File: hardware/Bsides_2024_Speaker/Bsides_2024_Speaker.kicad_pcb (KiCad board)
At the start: 2 copper layers, 144.4 x 144.3 mm, 45 parts, among them J1 Add_On, J2 Battery, J3 Battery, J4 OLED, J5 Serial_IN, J6 Serial_OUT, P1 USB_C_Plug_USB2.0, Q1 DMG3415U-7, SW1 ON, SW2 RESET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

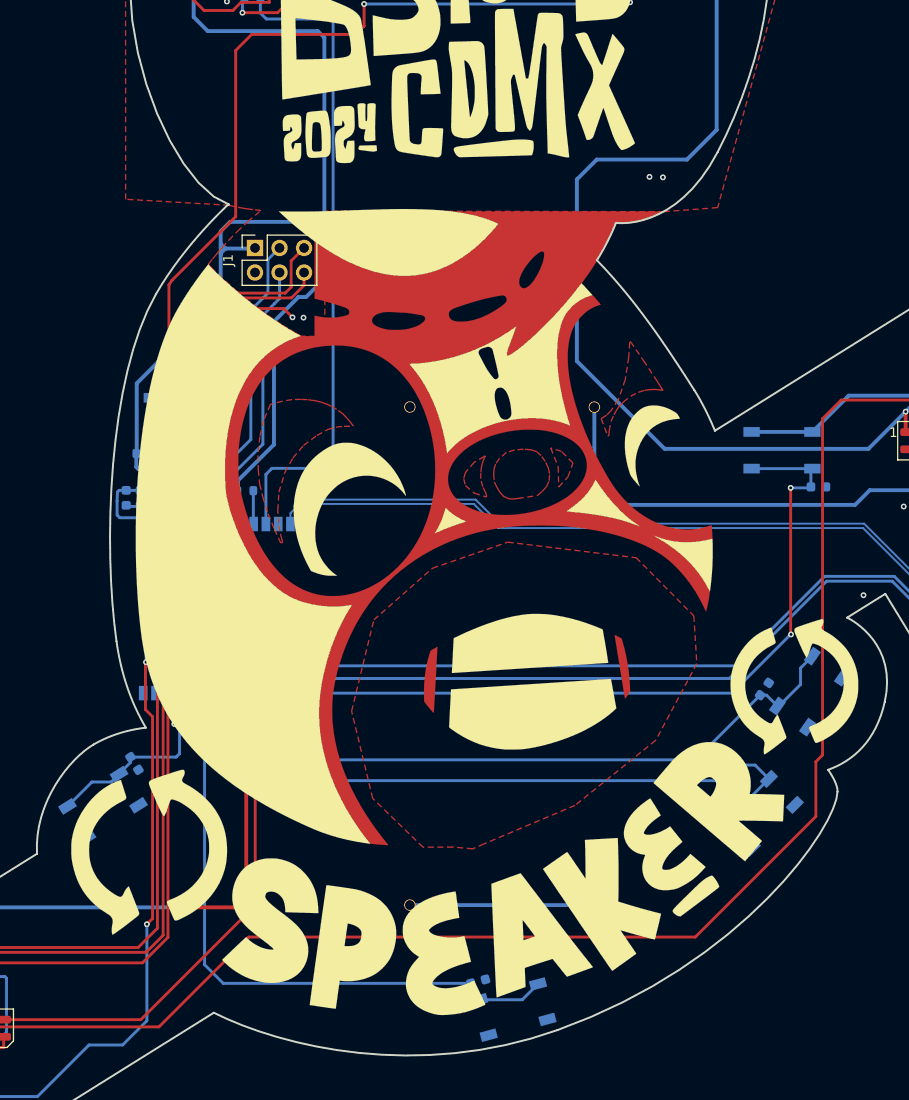
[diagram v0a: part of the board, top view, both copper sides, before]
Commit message: feat(Hw):Moved_Buttons_Speaker
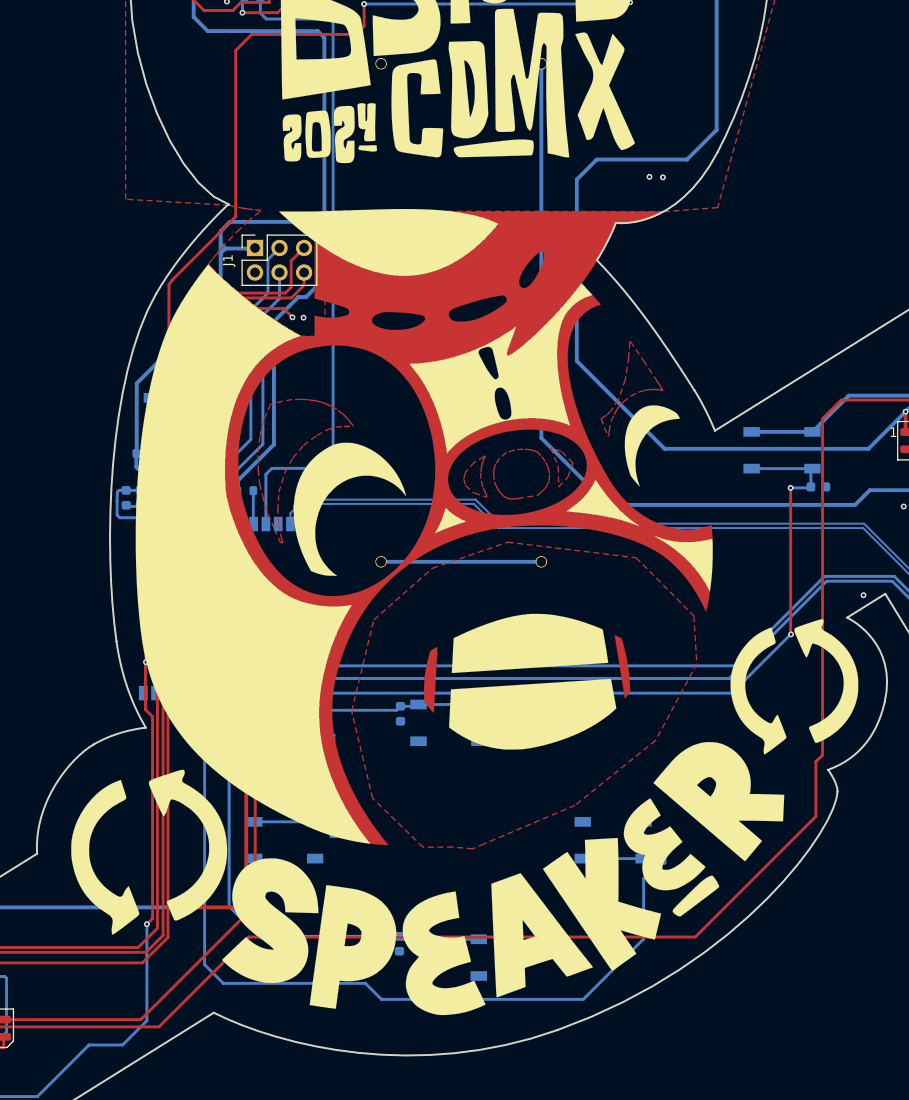
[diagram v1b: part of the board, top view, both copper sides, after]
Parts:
- moved C10 37.8 mm to (137.0, 120.1), turned to 90 degrees
- moved SW6 37.5 mm to (142.0, 121.0), turned to 0 degrees
- moved C11 37.5 mm to (136.9, 143.9), turned to 90 degrees
- moved J2 36.0 mm to (151.6, 78.6)
- moved J3 35.7 mm to (135.0, 78.6)
- moved SW7 35.6 mm to (141.9, 145.3), turned to 0 degrees
- moved C9 23.2 mm to (164.1, 134.5), turned to -90 degrees
- moved C8 21.7 mm to (130.1, 131.7), turned to 90 degrees
- moved SW5 20.3 mm to (159.0, 133.2), turned to 180 degrees
- moved SW4 19.1 mm to (125.0, 133.2), turned to 0 degrees
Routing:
- net /GPIO22: track 71.8 -> 26.5 mm
- net +BATT: track 51.1 -> 88.9 mm
- net /GPIO15: track 65.3 -> 94.8 mm
- net /GPIO23: track 71.1 -> 49.4 mm
- net /GPIO1: track 42.9 -> 59.3 mm
- net Net-(J2-Pin_1): track 19.1 -> 16.6 mm

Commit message: feat(Hw):Update_Csv_Speaker
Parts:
- added kibuzzard-666B311C: G***, kibuzzard-666B311C, B.Cu at (201.1, 97.0)
- added kibuzzard-666B3128: G***, kibuzzard-666B3128, F.Cu at (201.1, 97.0)
- added kibuzzard-666B314A: G***, kibuzzard-666B314A, F.Cu at (196.7, 89.8)
- added kibuzzard-666B316E: G***, kibuzzard-666B316E, B.Cu at (196.7, 89.7)
- added kibuzzard-666B3243: G***, kibuzzard-666B3243, B.Cu at (142.0, 124.8)
- added kibuzzard-666B3258: G***, kibuzzard-666B3258, B.Cu at (141.8, 141.4)
- added kibuzzard-666B327A: G***, kibuzzard-666B327A, B.Cu at (131.2, 134.0)
- added kibuzzard-666B328D: G***, kibuzzard-666B328D, B.Cu at (152.3, 133.0)
- F1: value 0.5A -> 0.75A
- SW2, SW4, SW6: value RESET -> SW
- SW5, SW7: value ~ -> SW
- moved J1 0.14 mm to (121.8, 71.8)
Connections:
- net /GPIO1 renamed /LEFT
- net /GPIO15 renamed /RIGHT
- net /GPIO16 renamed /TX
- net /GPIO17 renamed /RX
- net /GPIO22 renamed /UP
- net /GPIO23 renamed /DOWN
- net /GPIO4 renamed /RX1
- net /GPIO5 renamed /TX1
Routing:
- net GND: track 132.7 -> 122.7 mm

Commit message: feat(Hw): Update BOM
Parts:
- removed kibuzzard-666B3128: G***, kibuzzard-666B3128
- removed kibuzzard-666B314A: G***, kibuzzard-666B314A
- added kibuzzard-666B558C: G***, kibuzzard-666B558C, B.Cu at (176.4, 88.8)
- added kibuzzard-666B55CA: G***, kibuzzard-666B55CA, B.Cu at (152.3, 133.0)
- added kibuzzard-666B5A62: G***, kibuzzard-666B5A62, F.Cu at (203.7, 117.5)
- added kibuzzard-666B5A62: G***, kibuzzard-666B5A62, B.Cu at (84.4, 157.9)
- added kibuzzard-666B5A91: G***, kibuzzard-666B5A91, F.Cu at (206.2, 116.1)
- added kibuzzard-666B5A91: G***, kibuzzard-666B5A91, B.Cu at (85.7, 160.0)
- added kibuzzard-666B5AA1: G***, kibuzzard-666B5AA1, F.Cu at (208.1, 114.5)
- added kibuzzard-666B5AA1: G***, kibuzzard-666B5AA1, B.Cu at (83.3, 155.4)
- added kibuzzard-666B5BCA: G***, kibuzzard-666B5BCA, F.Cu at (121.7, 68.8)
- added kibuzzard-666B5C0A: G***, kibuzzard-666B5C0A, F.Cu at (121.7, 76.5)
- added kibuzzard-666B5C24: G***, kibuzzard-666B5C24, F.Cu at (124.3, 68.7)
- added kibuzzard-666B5C33: G***, kibuzzard-666B5C33, F.Cu at (124.3, 77.3)
- moved kibuzzard-666B328D 61.0 mm to (114.3, 85.4)
- moved J2 2.86 mm to (153.9, 76.9)
- moved J3 2.86 mm to (137.3, 76.9)
- moved D3 0.49 mm to (164.4, 41.4)
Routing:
- net GND: track 122.7 -> 116.1 mm, vias 11 -> 9
- net /VOUT: track 421.3 -> 424.4 mm
- net /RIGHT: track 94.8 -> 96.0 mm
- net +BATT: track 88.9 -> 89.6 mm
- net Net-(D4-DOUT): track 158.0 -> 158.6 mm
- net Net-(D3-DOUT): track 180.7 -> 180.2 mm

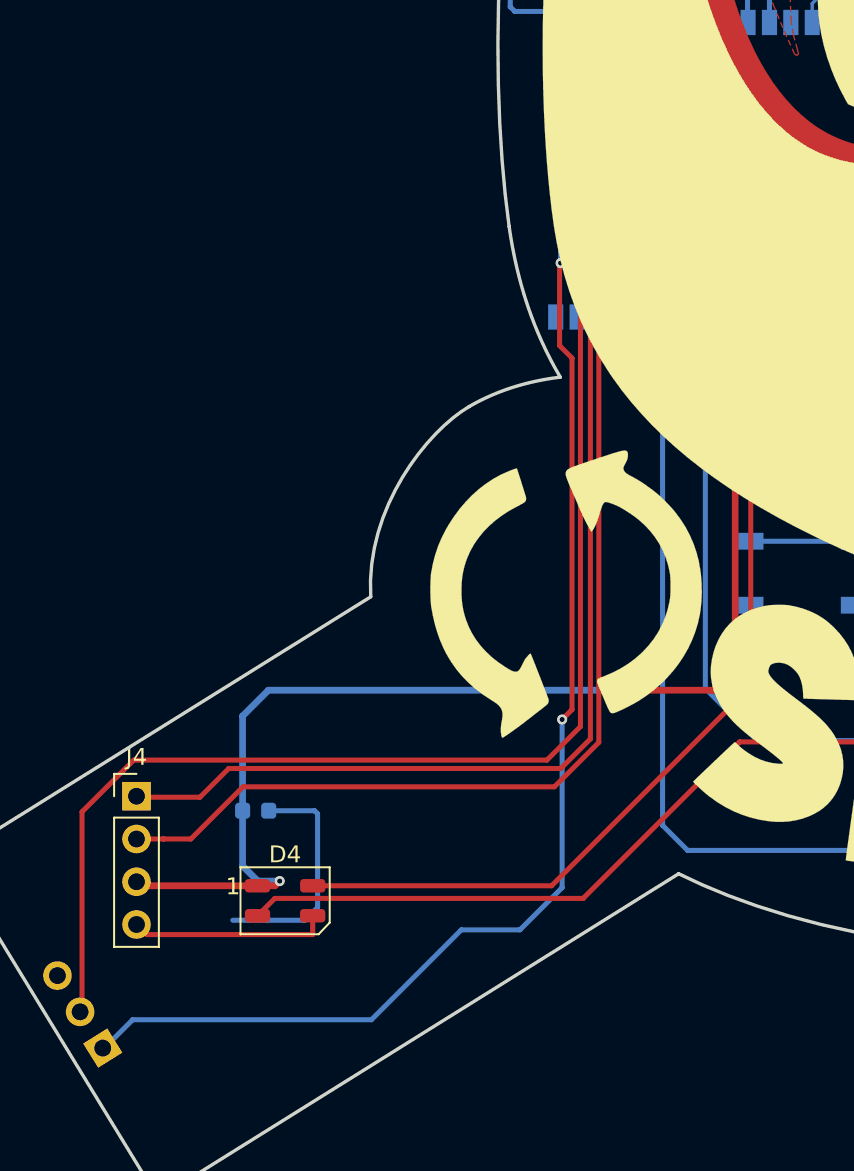
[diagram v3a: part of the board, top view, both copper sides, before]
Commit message: feat(Hw): Update route Speaker and Sponsor
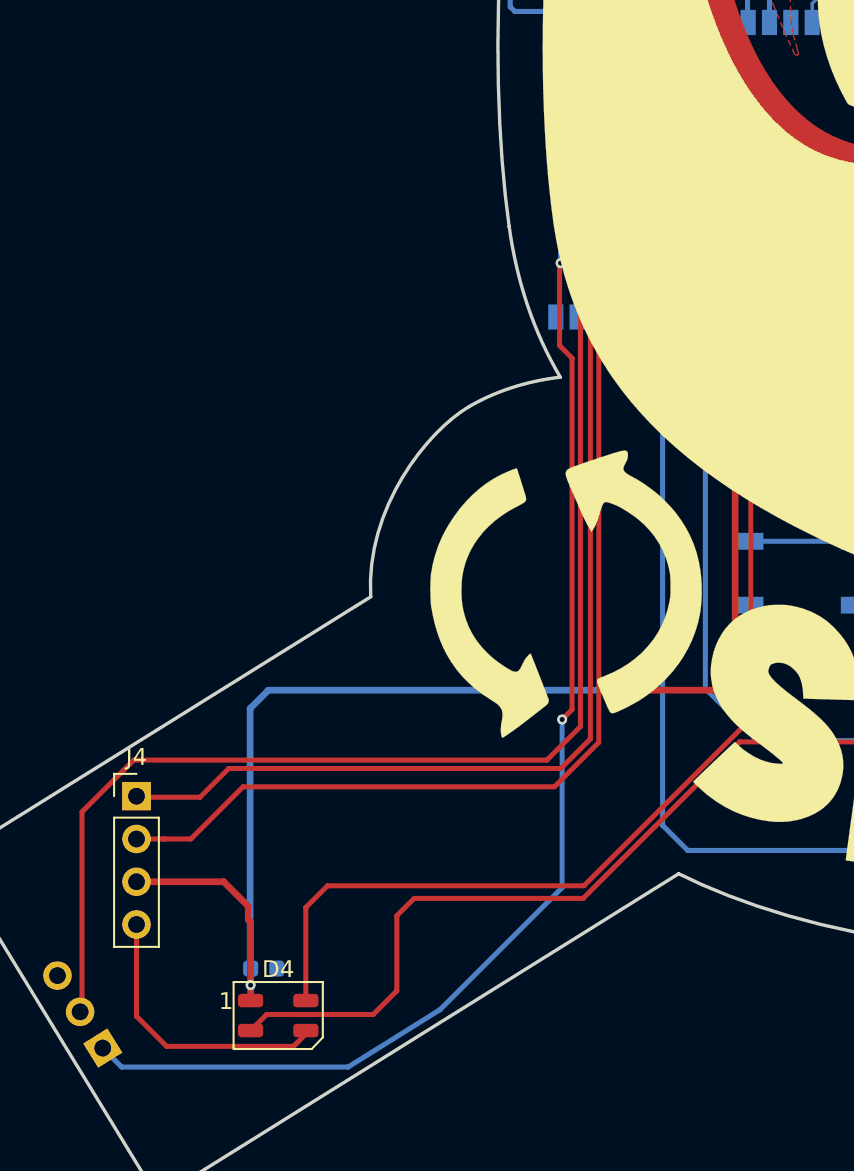
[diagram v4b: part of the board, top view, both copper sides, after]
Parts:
- moved C7 9.39 mm to (93.0, 156.6)
- moved D4 6.83 mm to (93.9, 159.4)
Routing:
- net GND: track 116.1 -> 107.1 mm
- net /VOUT: track 424.4 -> 432.9 mm
- net Net-(D3-DOUT): track 180.2 -> 187.8 mm
- net Net-(D4-DOUT): track 158.6 -> 164.4 mm

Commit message: feat(Hw): Labels added
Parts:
- moved J2 0.23 mm to (154.1, 76.9)
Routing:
- net +BATT: track 89.6 -> 91.0 mm
- net /VOUT: track 432.9 -> 433.9 mm
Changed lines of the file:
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@@
 	(footprint "bsides:BH-AA-A1AJ020"
 		(layer "B.Cu")
-		(at 153.88 76.875 -90)
+		(at 154.11 76.875 -90)
 		(property "Reference" "J2"
 			(at 0 0.5 90)
@@
 	)
 	(segment
-		(start 162.93 34.88)
-		(end 166.41 34.88)
-		(width 0.4)
-		(layer "B.Cu")
-		(net 3)
-	)
-	(segment
 		(start 111.52 98.485)
 		(end 111.4 98.605)
@@
 	)
 	(segment
-		(start 166.64 62.7)
-		(end 157.3 62.7)
+		(start 162.93 34.88)
+		(end 166.41 34.88)
 		(width 0.4)
 		(layer "B.Cu")
@@
 	)
 	(segment
+		(start 169.71 38.18)
+		(end 169.71 59.63)
+		(width 0.4)
+		(layer "B.Cu")
+		(net 3)
+	)
+	(segment
 		(start 118.38 72.39)
 		(end 118.38 72.49)
@@
 	)
 	(segment
-		(start 162.59 35.22)
-		(end 162.93 34.88)
-		(width 0.4)
-		(layer "B.Cu")
-		(net 3)
-	)
-	(segment
 		(start 160.55 42.9)
 		(end 158.97 44.48)
@@
 	)
 	(segment
-		(start 159.89 92.64)
-		(end 185.42 92.64)
+		(start 120.1775 95.9125)
+		(end 120.1775 96.8975)
 		(width 0.4)
 		(layer "B.Cu")
@@
 	)
 	(segment
-		(start 120.1775 95.9125)
-		(end 120.1775 96.8975)
+		(start 155.24 64.76)
+		(end 155.24 89.69)
 		(width 0.4)
 		(layer "B.Cu")
@@
 	)
 	(segment
-		(start 169.71 59.63)
-		(end 166.64 62.7)
-		(width 0.4)
-		(layer "B.Cu")
-		(net 3)
-	)
-	(segment
 		(start 93.29 140.1)
 		(end 115.2 140.1)
@@
 	)
 	(segment
-		(start 166.41 34.88)
-		(end 169.71 38.18)
-		(width 0.4)
-		(layer "B.Cu")
-		(net 3)
-	)
-	(segment
 		(start 111.85 94.74)
 		(end 112.4 95.29)
@@
 	)
 	(segment
-		(start 169.71 38.18)
-		(end 169.71 59.63)
+		(start 162.59 35.22)
+		(end 162.93 34.88)
 		(width 0.4)
 		(layer "B.Cu")
@@
 	)
 	(segment
+		(start 162.59 38.2)
+		(end 162.59 35.22)
+		(width 0.4)
+		(layer "B.Cu")
+		(net 3)
+	)
+	(segment
 		(start 128.7 69.22)
 		(end 128.7 69.08)
@@
 	)
 	(segment
+		(start 169.71 59.63)
+		(end 166.64 62.7)
+		(width 0.4)
+		(layer "B.Cu")
+		(net 3)
+	)
+	(segment
 		(start 118.86 71.91)
 		(end 121.73 71.91)
@@
 	)
 	(segment
-		(start 185.42 92.64)
-		(end 189.27 88.79)
+		(start 155.24 89.69)
+		(end 158.19 92.64)
 		(width 0.4)
 		(layer "B.Cu")
@@
 	)
 	(segment
+		(start 185.42 92.64)
+		(end 189.27 88.79)
+		(width 0.4)
+		(layer "B.Cu")
+		(net 3)
+	)
+	(segment
 		(start 120.48 44.48)
 		(end 119.91 43.91)
@@
 	)
 	(segment
-		(start 155.24 87.99)
-		(end 159.89 92.64)
-		(width 0.4)
-		(layer "B.Cu")
-		(net 3)
-	)
-	(segment
 		(start 157.3 62.7)
 		(end 155.24 64.76)
@@
 	)
 	(segment
+		(start 158.19 92.64)
+		(end 185.42 92.64)
+		(width 0.4)
+		(layer "B.Cu")
+		(net 3)
+	)
+	(segment
 		(start 92.235 156.64)
 		(end 92.2 156.605)
@@
 	)
 	(segment
-		(start 155.24 64.76)
-		(end 155.24 87.99)
+		(start 166.64 62.7)
+		(end 157.3 62.7)
 		(width 0.4)
 		(layer "B.Cu")
@@
 	)
 	(segment
-		(start 162.59 38.2)
-		(end 162.59 35.22)
-		(width 0.4)
-		(layer "B.Cu")
-		(net 3)
-	)
-	(segment
 		(start 193.065 88.01)
 		(end 193.065 92.27495)
@@
 	)
 	(segment
+		(start 166.41 34.88)
+		(end 169.71 38.18)
+		(width 0.4)
+		(layer "B.Cu")
+		(net 3)
+	)
+	(segment
 		(start 129.11 50.08)
 		(end 129.11 68.19)
@@
 	)
 	(segment
-		(start 184.04 98.44)
-		(end 185.56 96.92)
+		(start 154.11 51.1)
+		(end 154.11 96.16)
 		(width 0.4)
 		(layer "B.Cu")
@@
 	)
 	(segment
-		(start 153.88 93.84)
-		(end 158.48 98.44)
+		(start 154.11 96.16)
+		(end 156.39 98.44)
 		(width 0.4)
 		(layer "B.Cu")
@@
 	)
 	(segment
-		(start 153.891847 51.111847)
-		(end 153.88 51.1)
+		(start 153.903694 51.1)
+		(end 154.11 51.1)
+		(width 0.4)
+		(layer "B.Cu")
+		(net 20)
+	)
+	(segment
+		(start 185.56 96.92)
+		(end 198.235 96.92)
 		(width 0.4)
 		(layer "B.Cu")
@@
 	)
 	(segment
-		(start 158.48 98.44)
+		(start 156.39 98.44)
 		(end 184.04 98.44)
 		(width 0.4)
@@
 	)
 	(segment
-		(start 153.88 51.1)
-		(end 153.88 93.84)
+		(start 184.04 98.44)
+		(end 185.56 96.92)
 		(width 0.4)
 		(layer "B.Cu")
@@
 	)
 	(segment
-		(start 185.56 96.92)
-		(end 198.235 96.92)
+		(start 153.891847 51.111847)
+		(end 153.903694 51.1)
 		(width 0.4)
 		(layer "B.Cu")
@@
 	)
 	(segment
-		(start 153.879107 102.649107)
-		(end 153.88 102.65)
-		(width 0.2)
+		(start 154.109107 102.649107)
+		(end 154.11 102.65)
+		(width 0.4)
 		(layer "B.Cu")
 		(net 21)
@@
 	(segment
 		(start 137.288153 102.649107)
-		(end 153.879107 102.649107)
+		(end 154.109107 102.649107)
 		(width 0.4)
 		(layer "B.Cu")

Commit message: feat(Hw): Update labels
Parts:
- added kibuzzard-666B5BCA: G***, kibuzzard-666B5BCA, B.Cu at (137.3, 100.9)
- added kibuzzard-666B5BCA: G***, kibuzzard-666B5BCA, B.Cu at (154.1, 52.8)
- added kibuzzard-666B5C0A: G***, kibuzzard-666B5C0A, B.Cu at (154.1, 101.1)
- added kibuzzard-666B5C0A: G***, kibuzzard-666B5C0A, B.Cu at (137.3, 52.6)

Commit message: feat(Hw): Update labels
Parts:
- removed the kibuzzard-666B5BCA at (137.3, 100.9)
- removed the kibuzzard-666B5C0A at (154.1, 101.1)
- moved kibuzzard-666B5BCA 5.58 mm to (154.1, 47.2)
- moved kibuzzard-666B5C0A 5.38 mm to (137.3, 47.2)
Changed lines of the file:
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@@
 		)
 	)
-	(footprint "kibuzzard-666B5C0A"
-		(layer "B.Cu")
-		(at 154.09 101.1)
-		(descr "Generated with KiBuzzard")
-		(tags "kb_params=eyJBbGlnbm1lbnRDaG9pY2UiOiAiQ2VudGVyIiwgIkNhcExlZnRDaG9pY2UiOiAiWyIsICJDYXBSaWdodENob2ljZSI6ICJdIiwgIkZvbnRDb21ib0JveCI6ICJVYnVudHVNb25vLUIiLCAiSGVpZ2h0Q3RybCI6IDAuMiwgIkxheWVyQ29tYm9Cb3giOiAiRi5TaWxrUyIsICJMaW5lU3BhY2luZ0N0cmwiOiAyLjAsICJNdWx0aUxpbmVUZXh0IjogIi0iLCAiUGFkZGluZ0JvdHRvbUN0cmwiOiAyLjAsICJQYWRkaW5nTGVmdEN0cmwiOiAyLjAsICJQYWRkaW5nUmlnaHRDdHJsIjogMi4wLCAiUGFkZGluZ1RvcEN0cmwiOiAyLjAsICJXaWR0aEN0cmwiOiAwLjZ9")
-		(property "Reference" "kibuzzard-666B5C0A"
-			(at 0 3.423482 360)
-			(layer "B.SilkS")
-			(hide yes)
-			(effects
-				(font
-					(size 0.001 0.001)
-					(thickness 0.15)
-				)
-				(justify mirror)
-			)
-		)
-		(property "Value" "G***"
-			(at 0 -3.423482 360)
-			(layer "B.SilkS")
-			(hide yes)
-			(effects
-				(font
-					(size 0.001 0.001)
-					(thickness 0.15)
-				)
-				(justify mirror)
-			)
-		)
-		(property "Footprint" ""
-			(at 0 0 360)
-			(layer "B.Fab")
-			(hide yes)
-			(effects
-				(font
-					(size 1.27 1.27)
-					(thickness 0.15)
-				)
-				(justify mirror)
-			)
-		)
-		(property "Datasheet" ""
-			(at 0 0 360)
-			(layer "B.Fab")
-			(hide yes)
-			(effects
-				(font
-					(size 1.27 1.27)
-					(thickness 0.15)
-				)
-				(justify mirror)
-			)
-		)
-		(property "Description" ""
-			(at 0 0 360)
-			(layer "B.Fab")
-			(hide yes)
-			(effects
-				(font
-					(size 1.27 1.27)
-					(thickness 0.15)
-				)
-				(justify mirror)
-			)
-		)
-		(attr board_only exclude_from_pos_files exclude_from_bom)
-		(fp_poly
-			(pts
-				(xy -0.226446 0.375482) (xy -0.501928 0.375482) (xy -0.501928 -0.375482) (xy -0.226446 -0.375482)
-				(xy 0.226446 -0.375482) (xy 0.226446 -0.1) (xy -0.226446 -0.1) (xy -0.226446 0.1) (xy 0.226446 0.1)
-				(xy 0.226446 -0.1) (xy 0.226446 -0.375482) (xy 0.501928 -0.375482) (xy 0.501928 0.375482) (xy 0.226446 0.375482)
-				(xy -0.226446 0.375482)
-			)
-			(stroke
-				(width 0)
-				(type solid)
-			)
-			(fill solid)
-			(layer "B.SilkS")
-		)
-	)
 	(footprint "Capacitor_SMD:C_0603_1608Metric"
 		(layer "B.Cu")
@@
 		)
 	)
-	(footprint "kibuzzard-666B5BCA"
-		(layer "B.Cu")
-		(at 137.28 100.89 180)
-		(descr "Generated with KiBuzzard")
-		(tags "kb_params=eyJBbGlnbm1lbnRDaG9pY2UiOiAiQ2VudGVyIiwgIkNhcExlZnRDaG9pY2UiOiAiWyIsICJDYXBSaWdodENob2ljZSI6ICJdIiwgIkZvbnRDb21ib0JveCI6ICJVYnVudHVNb25vLUIiLCAiSGVpZ2h0Q3RybCI6IDEuMCwgIkxheWVyQ29tYm9Cb3giOiAiRi5TaWxrUyIsICJMaW5lU3BhY2luZ0N0cmwiOiAxLjUsICJNdWx0aUxpbmVUZXh0IjogIisiLCAiUGFkZGluZ0JvdHRvbUN0cmwiOiAxLjAsICJQYWRkaW5nTGVmdEN0cmwiOiAyLjUsICJQYWRkaW5nUmlnaHRDdHJsIjogMi41LCAiUGFkZGluZ1RvcEN0cmwiOiAxLjAsICJXaWR0aEN0cmwiOiAxLjB9")
-		(property "Reference" "kibuzzard-666B5BCA"
-			(at 0 3.733598 360)
-			(layer "B.SilkS")
-			(hide yes)
-			(effects
-				(font
-					(size 0.001 0.001)
-					(thickness 0.15)
-				)
-				(justify mirror)
-			)
-		)
-		(property "Value" "G***"
-			(at 0 -3.733598 360)
-			(layer "B.SilkS")
-			(hide yes)
-			(effects
-				(font
-					(size 0.001 0.001)
-					(thickness 0.15)
-				)
-				(justify mirror)
-			)
-		)
-		(property "Footprint" ""
-			(at 0 0 360)
-			(layer "B.Fab")
-			(hide yes)
-			(effects
-				(font
-					(size 1.27 1.27)
-					(thickness 0.15)
-				)
-				(justify mirror)
-			)
-		)
-		(property "Datasheet" ""
-			(at 0 0 360)
-			(layer "B.Fab")
-			(hide yes)
-			(effects
-				(font
-					(size 1.27 1.27)
-					(thickness 0.15)
-				)
-				(justify mirror)
-			)
-		)
-		(property "Description" ""
-			(at 0 0 360)
-			(layer "B.Fab")
-			(hide yes)
-			(effects
-				(font
-					(size 1.27 1.27)
-					(thickness 0.15)
-				)
-				(justify mirror)
-			)
-		)
-		(attr board_only exclude_from_pos_files exclude_from_bom)
-		(fp_poly
-			(pts
-				(xy -0.467706 0.685598) (xy -0.9317 0.685598) (xy -0.9317 -0.685598) (xy -0.467706 -0.685598) (xy 0.11804 -0.685598)
-				(xy 0.11804 -0.5) (xy -0.11804 -0.5) (xy -0.11804 -0.112472) (xy -0.467706 -0.112472) (xy -0.467706 0.112472)
-				(xy -0.11804 0.112472) (xy -0.11804 0.5) (xy 0.11804 0.5) (xy 0.11804 0.112472) (xy 0.467706 0.112472)
-				(xy 0.467706 -0.112472) (xy 0.11804 -0.112472) (xy 0.11804 -0.5) (xy 0.11804 -0.685598) (xy 0.467706 -0.685598)
-				(xy 0.9317 -0.685598) (xy 0.9317 0.685598) (xy 0.467706 0.685598) (xy -0.467706 0.685598)
-			)
-			(stroke
-				(width 0)
-				(type solid)
-			)
-			(fill solid)
-			(layer "B.SilkS")
-		)
-	)
 	(footprint "Resistor_SMD:R_0603_1608Metric"
 		(layer "B.Cu")
@@
 	(footprint "kibuzzard-666B5BCA"
 		(layer "B.Cu")
-		(at 154.14 52.78)
+		(at 154.14 47.2)
 		(descr "Generated with KiBuzzard")
 		(tags "kb_params=eyJBbGlnbm1lbnRDaG9pY2UiOiAiQ2VudGVyIiwgIkNhcExlZnRDaG9pY2UiOiAiWyIsICJDYXBSaWdodENob2ljZSI6ICJdIiwgIkZvbnRDb21ib0JveCI6ICJVYnVudHVNb25vLUIiLCAiSGVpZ2h0Q3RybCI6IDEuMCwgIkxheWVyQ29tYm9Cb3giOiAiRi5TaWxrUyIsICJMaW5lU3BhY2luZ0N0cmwiOiAxLjUsICJNdWx0aUxpbmVUZXh0IjogIisiLCAiUGFkZGluZ0JvdHRvbUN0cmwiOiAxLjAsICJQYWRkaW5nTGVmdEN0cmwiOiAyLjUsICJQYWRkaW5nUmlnaHRDdHJsIjogMi41LCAiUGFkZGluZ1RvcEN0cmwiOiAxLjAsICJXaWR0aEN0cmwiOiAxLjB9")
@@
 	(footprint "kibuzzard-666B5C0A"
 		(layer "B.Cu")
-		(at 137.29 52.56 180)
+		(at 137.26 47.18 180)
 		(descr "Generated with KiBuzzard")
 		(tags "kb_params=eyJBbGlnbm1lbnRDaG9pY2UiOiAiQ2VudGVyIiwgIkNhcExlZnRDaG9pY2UiOiAiWyIsICJDYXBSaWdodENob2ljZSI6ICJdIiwgIkZvbnRDb21ib0JveCI6ICJVYnVudHVNb25vLUIiLCAiSGVpZ2h0Q3RybCI6IDAuMiwgIkxheWVyQ29tYm9Cb3giOiAiRi5TaWxrUyIsICJMaW5lU3BhY2luZ0N0cmwiOiAyLjAsICJNdWx0aUxpbmVUZXh0IjogIi0iLCAiUGFkZGluZ0JvdHRvbUN0cmwiOiAyLjAsICJQYWRkaW5nTGVmdEN0cmwiOiAyLjAsICJQYWRkaW5nUmlnaHRDdHJsIjogMi4wLCAiUGFkZGluZ1RvcEN0cmwiOiAyLjAsICJXaWR0aEN0cmwiOiAwLjZ9")
